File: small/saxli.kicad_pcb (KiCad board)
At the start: 4 copper layers, 160.5 x 102.4 mm, 207 parts, among them IC1 PIC32MX350F256H-V_PT, IC2 SIM808, J1 78800-0001, J10 Conn_01x06_Female, J11 Conn_Coaxial, J12 Conn_Coaxial, J2 Screw_Terminal_01x02, J3 Micro_SD_Card, J4 Conn_01x05_Female, J5 Conn_02x04_Odd_Even, J6 RJ45_Amphenol_RJMG1BD3B8K1ANR, J7 Screw_Terminal_01x08, J8 Screw_Terminal_01x08, J9 Screw_Terminal_01x08, Q1 2N7002, Q2 2N7002, Q3 2N7002, Q4 AO3401A, U1 LM358, U10 TPS5430DDAR, U11 EL357N(C)(TA)-G, U12 EL357N(C)(TA)-G, U13 ASSR-1218, U14 ST485EBDR, U15 ASSR-1218, U16 SRV05-4, U18 ULN2003A, U2 LM7805_TO220, U20 TPS5430DDAR, U4 ENC28J60x-SS, U5 AT25M02, U6 EL357N(C)(TA)-G, U7 EL357N(C)(TA)-G, U8 PCF8563T, U9 ISO1540, Y1 YSX321SL, Y2 Crystal

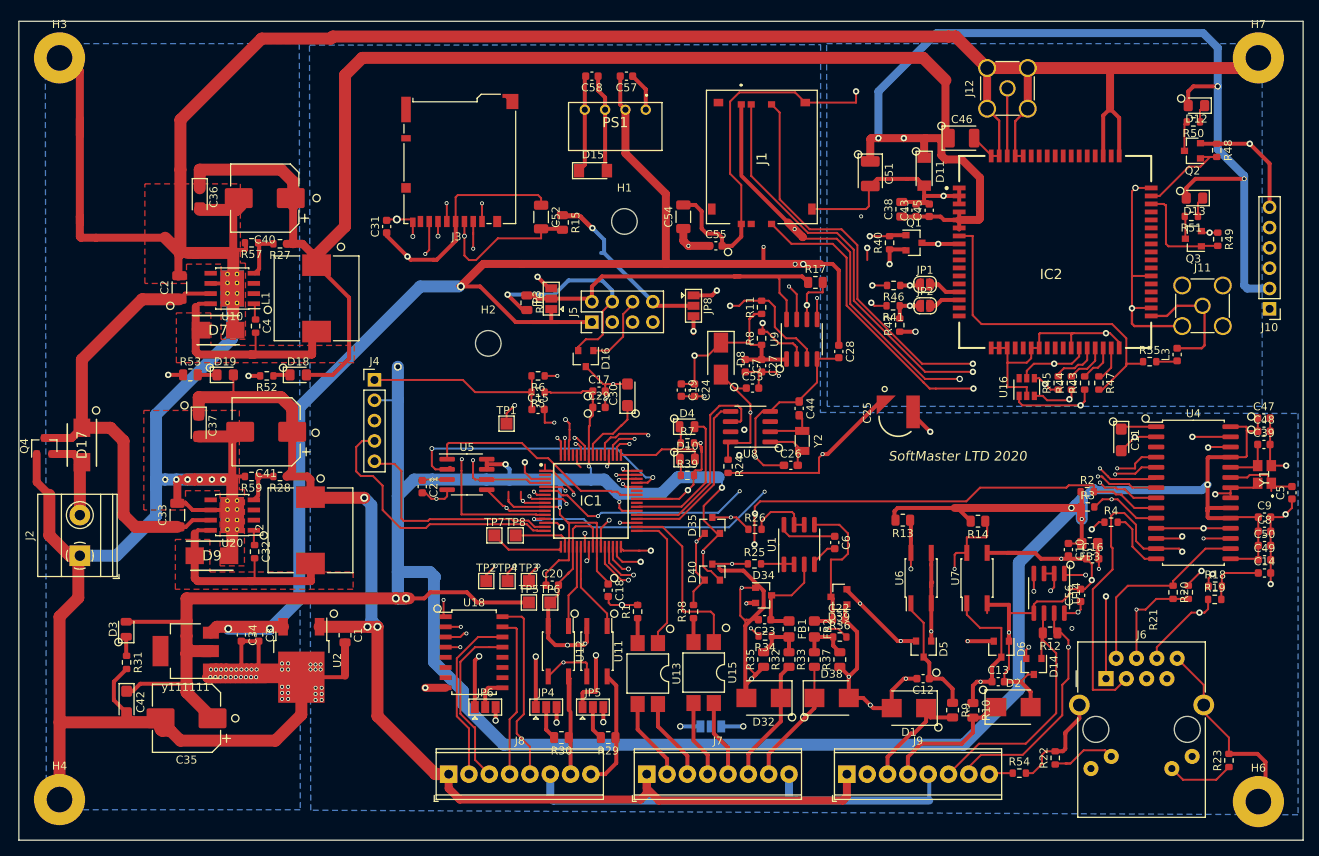
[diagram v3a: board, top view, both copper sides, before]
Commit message: accelerometer added
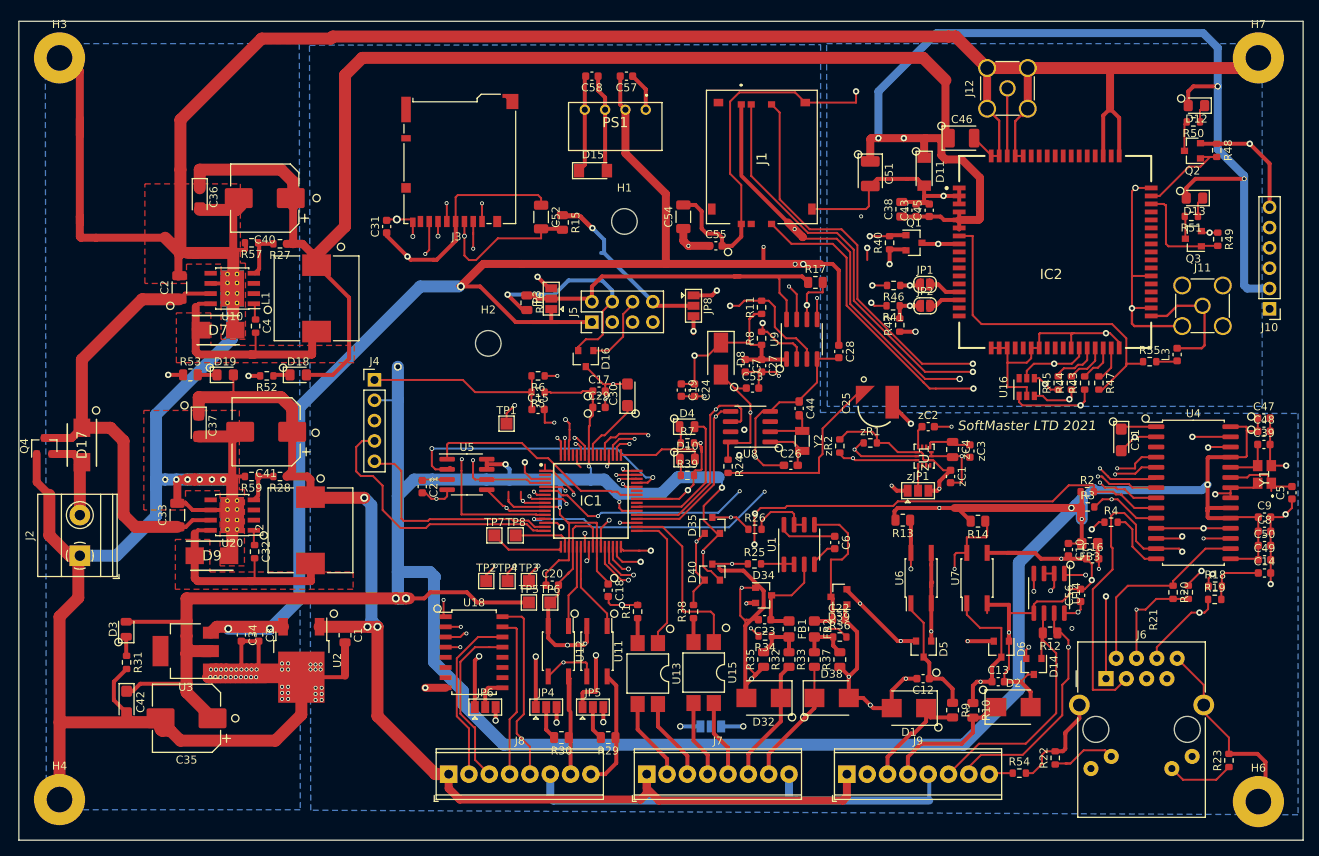
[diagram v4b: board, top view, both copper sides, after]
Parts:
- added zC1: 10n, Capacitor_SMD:C_0603_1608Metric, F.Cu at (154.6, 77.7)
- added zC2: 0.1u, Capacitor_SMD:C_0603_1608Metric, F.Cu at (151.8, 71.5)
- added zC3: 0.1u, Capacitor_SMD:C_0603_1608Metric, F.Cu at (157.0, 74.5)
- added zC4: C, Capacitor_SMD:C_0805_2012Metric, F.Cu at (154.8, 74.4)
- added zJP1: Jumper_NC_Dual, Jumper:SolderJumper-3_P1.3mm_Open_Pad1.0x1.5mm, F.Cu at (150.5, 79.5)
- added zR1: 5.1k, Resistor_SMD:R_0603_1608Metric, F.Cu at (144.5, 73.5)
- added zR2: 5.1k, Resistor_SMD:R_0603_1608Metric, F.Cu at (140.7, 73.9)
- added zU1: ICM-20600, small:ICM20600, F.Cu at (151.3, 75.2)
- moved C25 2.88 mm to (145.4, 69.1)
- renumbered у111111 to U3
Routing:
- net SCL1: track 27.3 -> 57.0 mm, vias 0 -> 2
- net SDA1: track 22.1 -> 51.6 mm, vias 0 -> 2
- net VDD3: track 571.4 -> 595.2 mm, vias 15 -> 17
- net GND: track 1196.3 -> 1210.4 mm, vias 98 -> 101
- net Net-(zC3-Pad1): track 0.00 -> 5.66 mm
- net U3RXSIM800: track 73.2 -> 77.3 mm
- net U3TXSIM800: track 64.7 -> 68.5 mm
- net Net-(zC2-Pad1): track 0.00 -> 2.73 mm
- net Net-(zJP1-Pad2): track 0.00 -> 2.54 mm
- net VDD5: track 423.5 -> 424.1 mm
- net ENC_SS: track 85.5 -> 84.9 mm
- net Net-(C30-Pad1): track 8.70 -> 8.18 mm
- net BATTERY: track 24.2 -> 23.8 mm, vias 1 -> 0
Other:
- board text added: "SoftMaster LTD 2021"
- board text removed: "SoftMaster LTD 2020"

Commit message: ULN2003 footprint updated
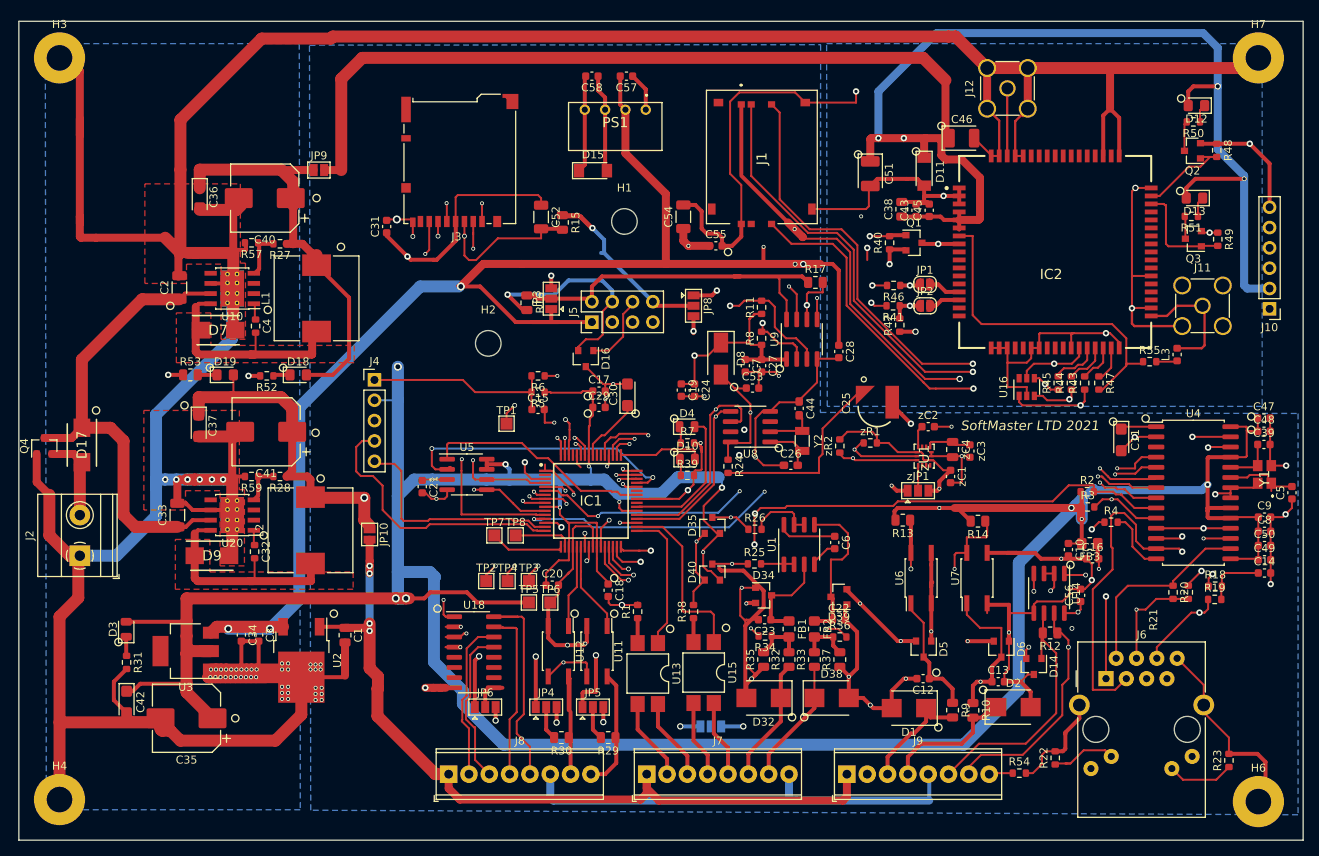
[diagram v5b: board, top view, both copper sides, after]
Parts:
- added JP10: Jumper, Jumper:SolderJumper-2_P1.3mm_Open_Pad1.0x1.5mm, F.Cu at (81.9, 85.0)
- added JP9: Jumper, Jumper:SolderJumper-2_P1.3mm_Open_Pad1.0x1.5mm, F.Cu at (75.6, 39.4)
- R57: value 3.24k -> 4.3k
- U18: footprint Package_SO:SOIC-16W_5.3x10.2mm_P1.27mm -> Package_SO:SOIC-16_3.9x9.9mm_P1.27mm
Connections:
- C36 pad 1: POWER_SIM -> Net-(C36-Pad1)
- C37 pad 1: 12V -> Net-(C37-Pad1)
- C40 pad 1: POWER_SIM -> Net-(C36-Pad1)
- C41 pad 1: 12V -> Net-(C37-Pad1)
- D18 pad 2: POWER_SIM -> Net-(C36-Pad1)
- D19 pad 2: 12V -> Net-(C37-Pad1)
- L1 pad 2: POWER_SIM -> Net-(C36-Pad1)
- L2 pad 2: 12V -> Net-(C37-Pad1)
- R27 pad 1: POWER_SIM -> Net-(C36-Pad1)
- R28 pad 1: 12V -> Net-(C37-Pad1)
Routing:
- net 12V: track 221.4 -> 153.1 mm, vias 7 -> 8
- net POWER_SIM: track 300.1 -> 241.1 mm
- net Net-(C36-Pad1): track 0.00 -> 53.3 mm
- net Net-(C37-Pad1): track 0.00 -> 41.9 mm, vias 0 -> 1
- net VDD3: track 595.2 -> 588.6 mm
- net RELAY_3: track 23.3 -> 26.2 mm
- net RELAY_2: track 20.4 -> 22.9 mm
- net RELAY_0: track 21.6 -> 19.2 mm
- net GND: track 1210.4 -> 1212.4 mm
- net VDD5: track 424.1 -> 422.2 mm
- net RELAY_1: track 21.9 -> 20.3 mm
- net 5V_IS: track 37.9 -> 36.5 mm
- net OUT_0: track 38.8 -> 39.9 mm
